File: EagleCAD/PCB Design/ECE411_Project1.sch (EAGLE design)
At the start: 39 parts, among them U2 MIC29310-5.0WU, U3 NCP5501DT50RKG, U4 DCJACK_2.1MM_PTH

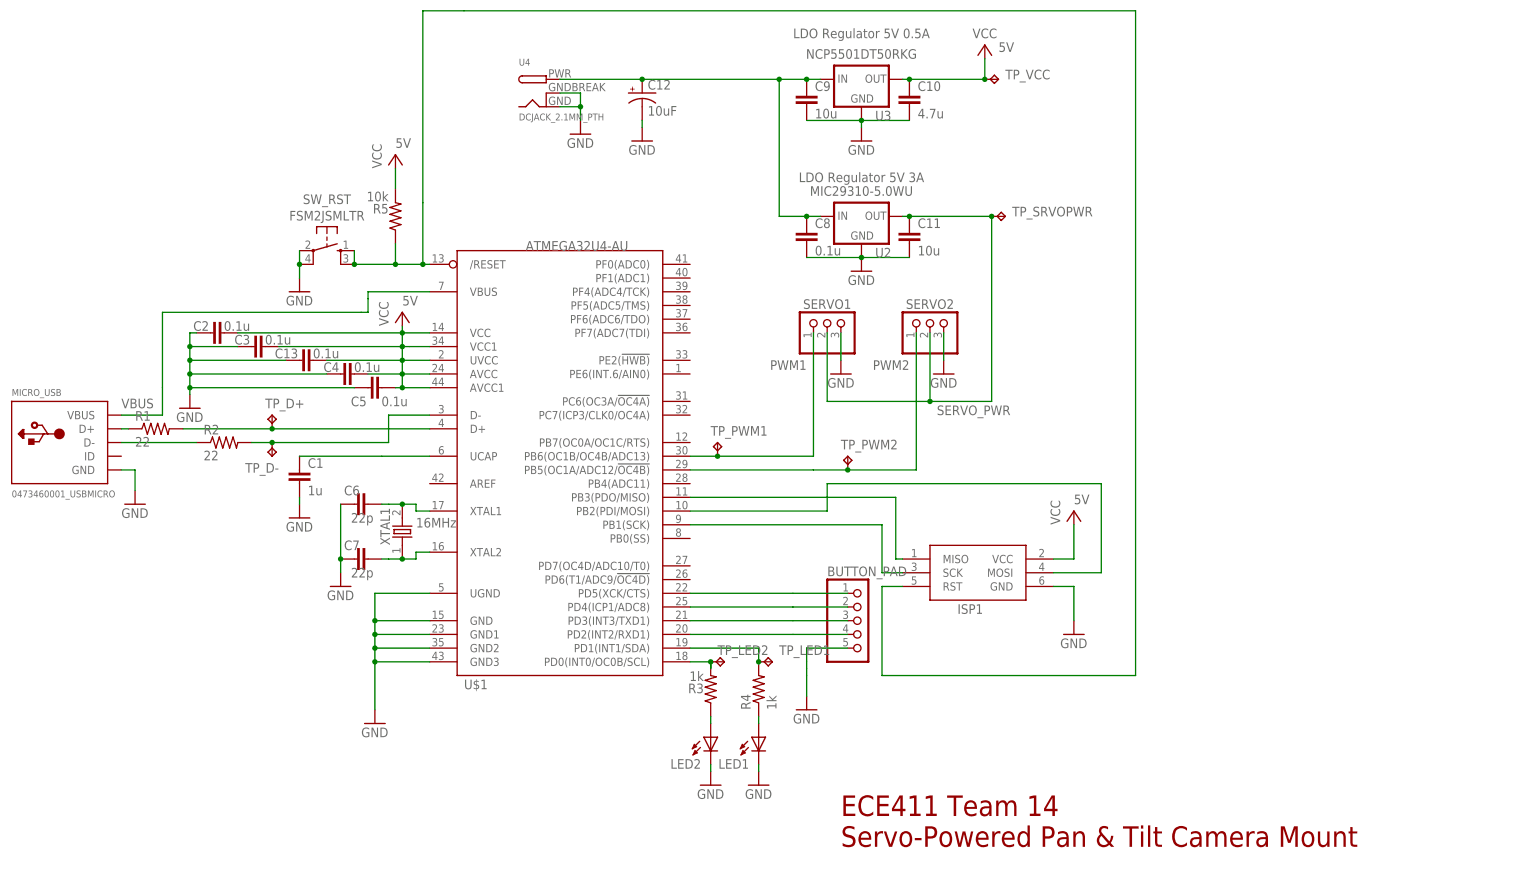
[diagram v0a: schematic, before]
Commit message: Updated the Board Layout: Added stitching vias, double gnd planes, set isolate distance to 10mils, smashed all the components and made their tnames look cohesive.
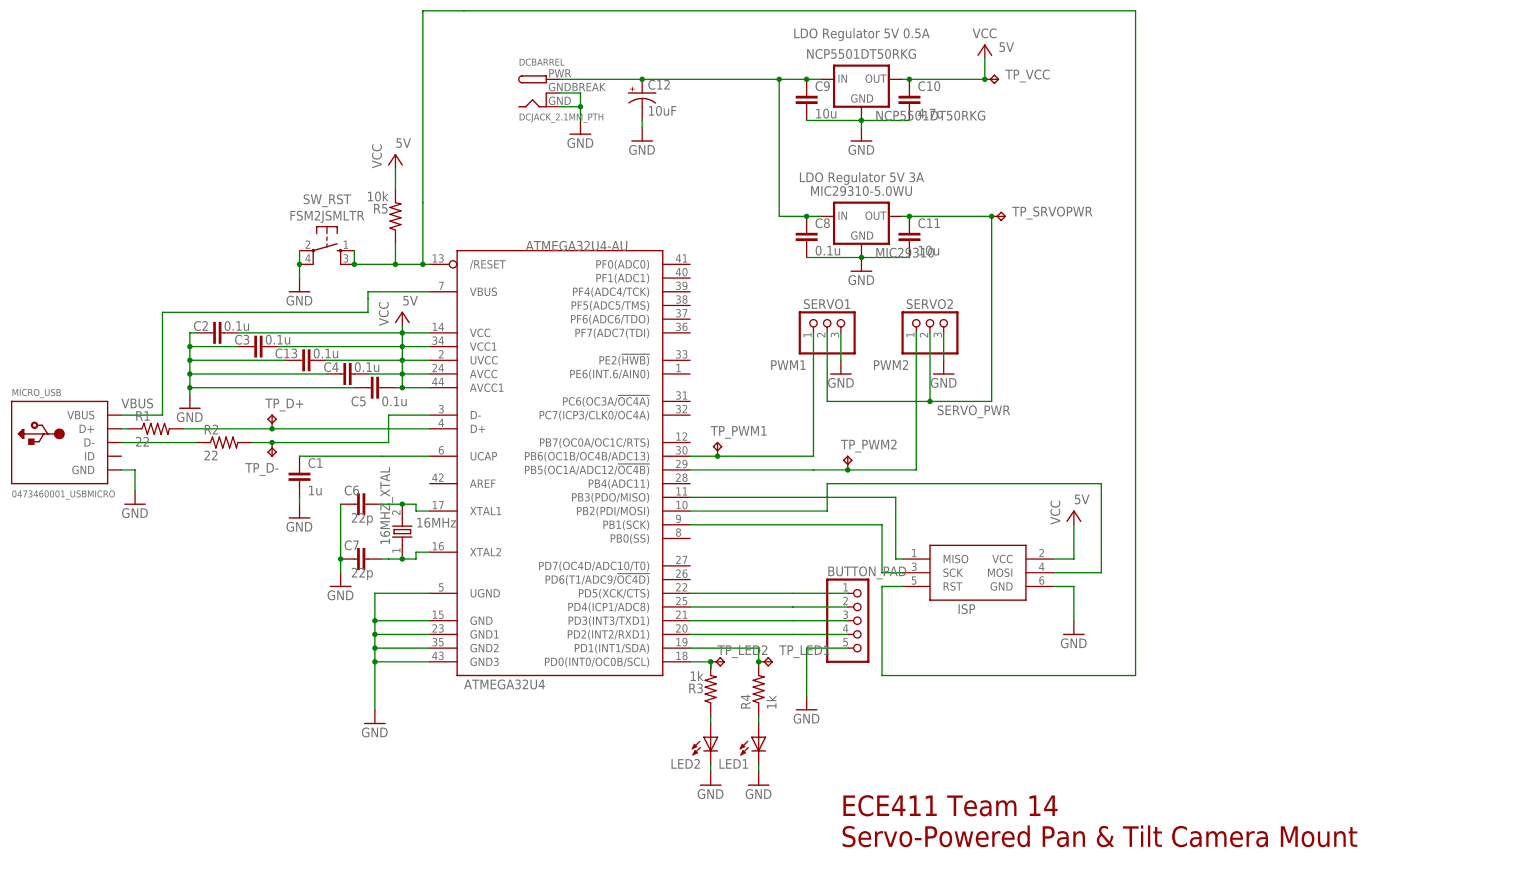
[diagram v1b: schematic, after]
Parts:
- renumbered ISP1 to ISP, U$1 to ATMEGA32U4, U2 to MIC29310, U3 to NCP5501DT50RKG, U4 to DCBARREL, XTAL1 to 16MHZ_XTAL

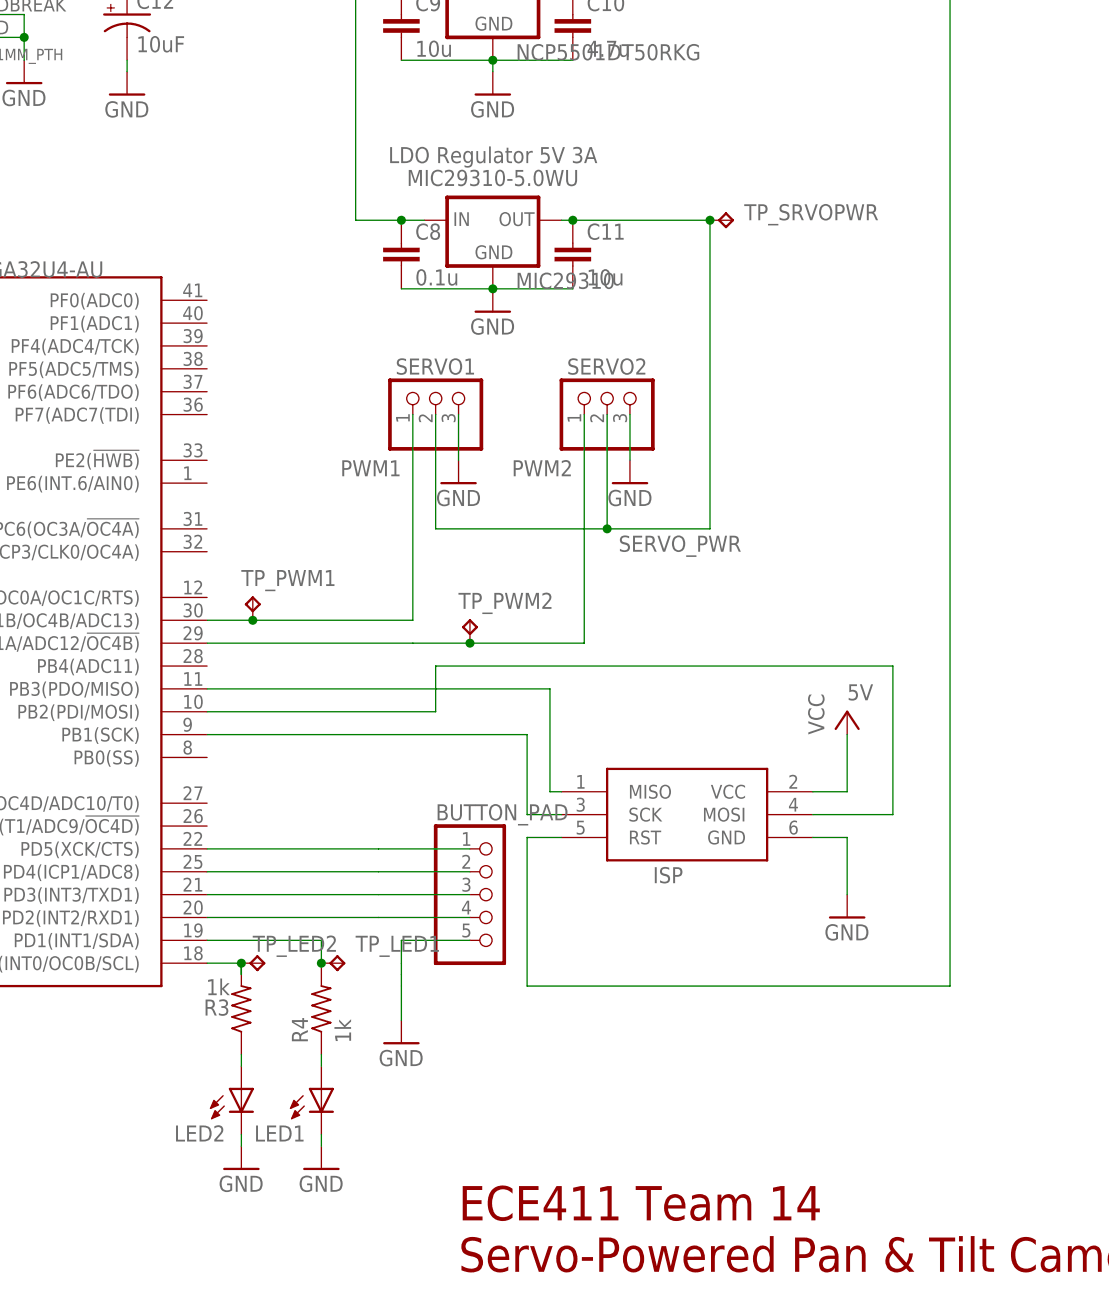
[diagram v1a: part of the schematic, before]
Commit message: Changed the schematic: moved the LEDs, and outputted the whole D port to a 9-pin header, with the ninth pin going to ground for the button pad.
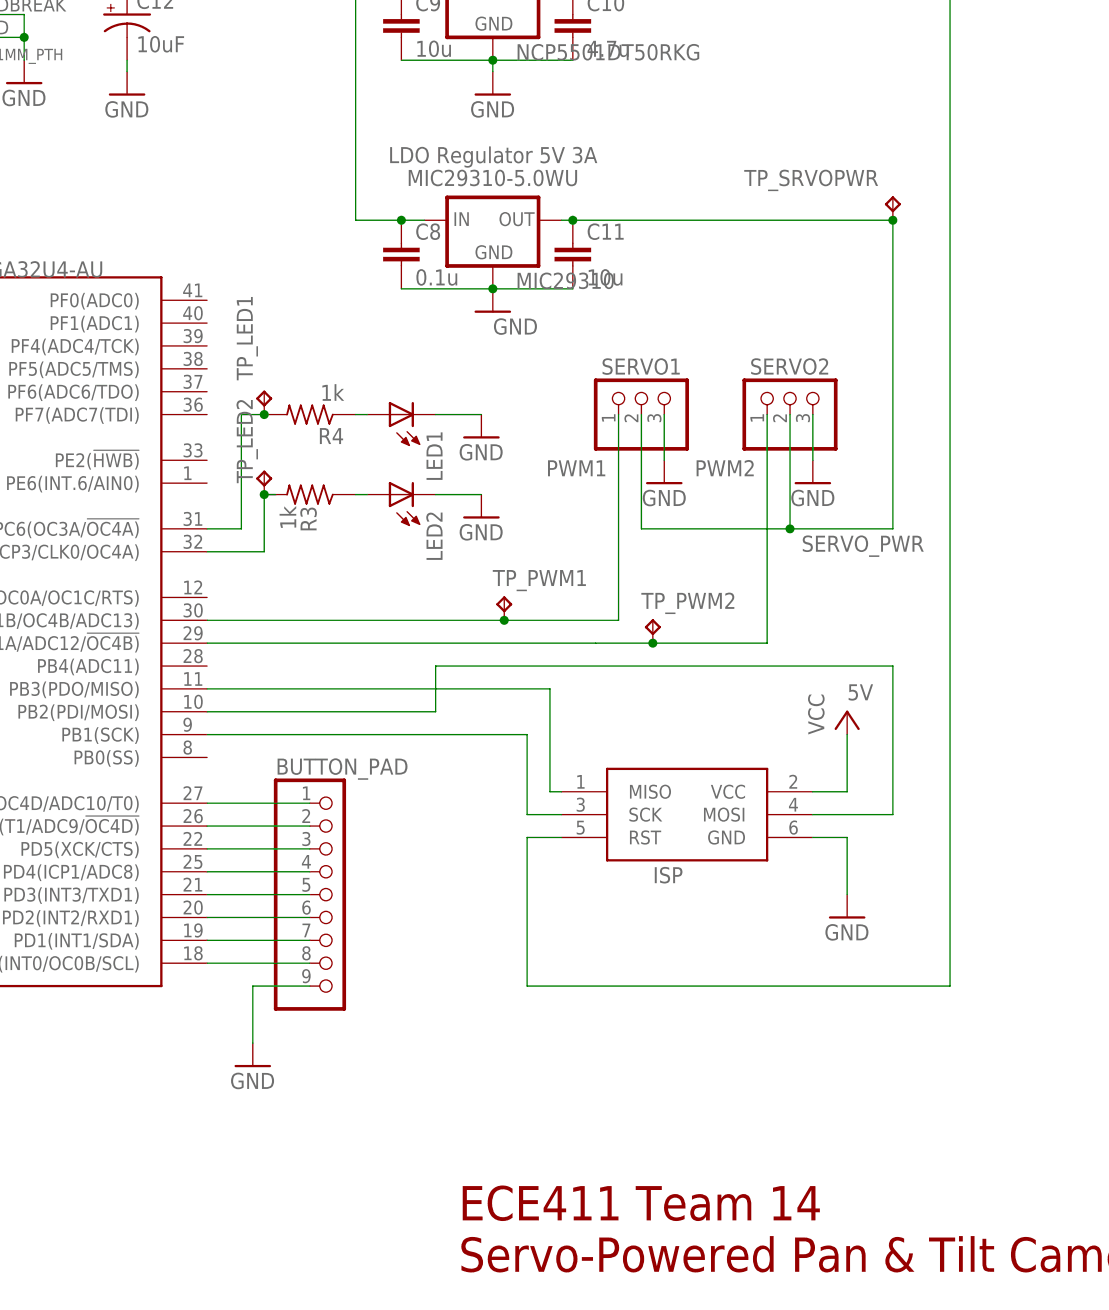
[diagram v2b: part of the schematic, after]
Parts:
- BUTTON_PAD: device pinhead:PINHD-1X5 -> pinhead:PINHD-1X9
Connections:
- removed net N$13: ATMEGA32U4.PD5(XCK/CTS), BUTTON_PAD.1
- new net N$1: ATMEGA32U4.PD7(OC4D/ADC10/T0), BUTTON_PAD.1
- new net N$2: ATMEGA32U4.PD6(T1/ADC9/!OC4D), BUTTON_PAD.2
- new net N$3: ATMEGA32U4.PD5(XCK/CTS), BUTTON_PAD.3
- new net N$4: ATMEGA32U4.PD4(ICP1/ADC8), BUTTON_PAD.4
- new net N$5: ATMEGA32U4.PD3(INT3/TXD1), BUTTON_PAD.5
- net GND: now also BUTTON_PAD.9; no longer BUTTON_PAD.5
- net N$11: now also ATMEGA32U4.PD1(INT1/SDA), BUTTON_PAD.7; no longer ATMEGA32U4.PD3(INT3/TXD1), BUTTON_PAD.3
- net N$12: now also ATMEGA32U4.PD0(INT0/OC0B/SCL), BUTTON_PAD.8; no longer ATMEGA32U4.PD4(ICP1/ADC8), BUTTON_PAD.2
- net N$6: now also ATMEGA32U4.PC7(ICP3/CLK0/OC4A); no longer ATMEGA32U4.PD0(INT0/OC0B/SCL)
- net N$7: now also BUTTON_PAD.6; no longer BUTTON_PAD.4
- net N$8: now also ATMEGA32U4.PC6(OC3A/!OC4A); no longer ATMEGA32U4.PD1(INT1/SDA)
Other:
- moved on the sheet: LED1, LED2, R3, R4, SERVO1, SERVO2, TP_LED1, TP_LED2, TP_PWM1, TP_PWM2, TP_SRVOPWR

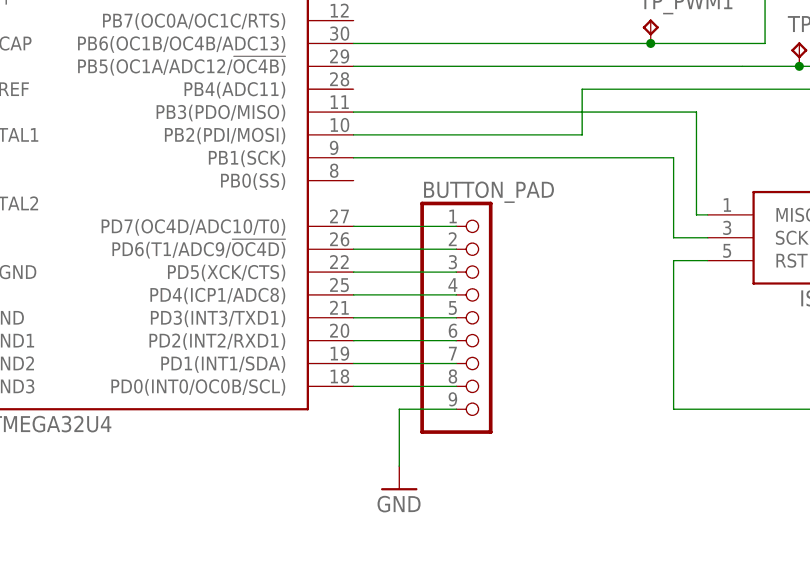
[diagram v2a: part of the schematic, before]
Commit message: Updated the schematic and the layout to output port D.
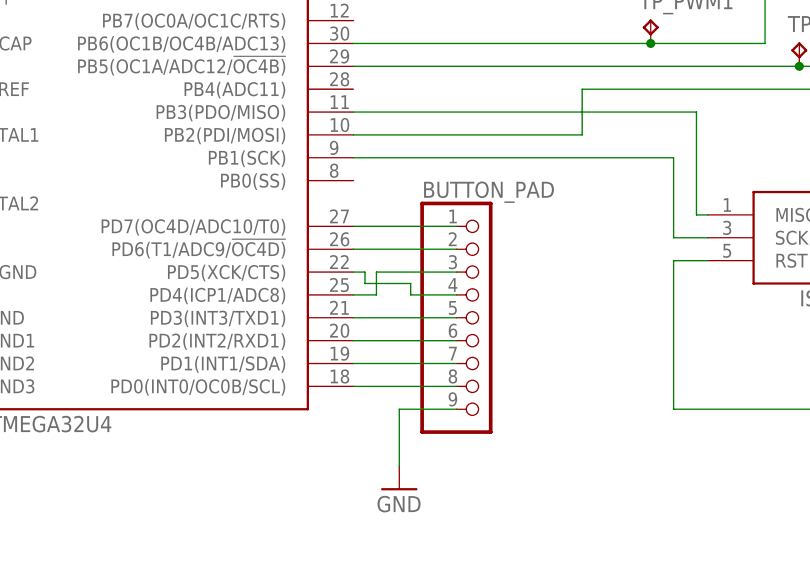
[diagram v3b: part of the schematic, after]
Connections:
- net N$6 renamed CHIP_LED2
- net N$8 renamed CHIP_LED1
- net N$3: now also ATMEGA32U4.PD4(ICP1/ADC8); no longer ATMEGA32U4.PD5(XCK/CTS)
- net N$4: now also ATMEGA32U4.PD5(XCK/CTS); no longer ATMEGA32U4.PD4(ICP1/ADC8)
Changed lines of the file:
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@@
 </segment>
 </net>
-<net name="N$6" class="0">
+<net name="CHIP_LED2" class="0">
 <segment>
 <wire x1="34.29" y1="62.23" x2="33.02" y2="62.23" width="0.1524" layer="91"/>
@@
 </segment>
 </net>
-<net name="N$8" class="0">
+<net name="CHIP_LED1" class="0">
 <segment>
 <pinref part="R4" gate="G$1" pin="2"/>
@@
 </segment>
 </net>
-<net name="N$3" class="0">
-<segment>
-<pinref part="BUTTON_PAD" gate="A" pin="3"/>
-<pinref part="ATMEGA32U4" gate="G$1" pin="PD5(XCK/CTS)"/>
-<wire x1="38.1" y1="22.86" x2="26.67" y2="22.86" width="0.1524" layer="91"/>
-</segment>
-</net>
-<net name="N$4" class="0">
-<segment>
-<pinref part="BUTTON_PAD" gate="A" pin="4"/>
-<pinref part="ATMEGA32U4" gate="G$1" pin="PD4(ICP1/ADC8)"/>
-<wire x1="38.1" y1="20.32" x2="26.67" y2="20.32" width="0.1524" layer="91"/>
-</segment>
-</net>
 <net name="N$5" class="0">
 <segment>
@@
 </segment>
 </net>
+<net name="N$3" class="0">
+<segment>
+<pinref part="ATMEGA32U4" gate="G$1" pin="PD4(ICP1/ADC8)"/>
+<wire x1="26.67" y1="20.32" x2="29.21" y2="20.32" width="0.1524" layer="91"/>
+<wire x1="29.21" y1="20.32" x2="29.21" y2="22.86" width="0.1524" layer="91"/>
+<pinref part="BUTTON_PAD" gate="A" pin="3"/>
+<wire x1="29.21" y1="22.86" x2="38.1" y2="22.86" width="0.1524" layer="91"/>
+</segment>
+</net>
+<net name="N$4" class="0">
+<segment>
+<pinref part="ATMEGA32U4" gate="G$1" pin="PD5(XCK/CTS)"/>
+<wire x1="26.67" y1="22.86" x2="27.94" y2="22.86" width="0.1524" layer="91"/>
+<wire x1="27.94" y1="22.86" x2="27.94" y2="21.59" width="0.1524" layer="91"/>
+<wire x1="27.94" y1="21.59" x2="30.48" y2="21.59" width="0.1524" layer="91"/>
+<wire x1="30.48" y1="21.59" x2="33.02" y2="21.59" width="0.1524" layer="91"/>
+<wire x1="33.02" y1="21.59" x2="33.02" y2="20.32" width="0.1524" layer="91"/>
+<pinref part="BUTTON_PAD" gate="A" pin="4"/>
+<wire x1="33.02" y1="20.32" x2="38.1" y2="20.32" width="0.1524" layer="91"/>
+</segment>
+</net>
